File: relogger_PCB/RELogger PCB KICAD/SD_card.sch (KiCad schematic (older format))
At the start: 3 parts, among them J1 CON-SD-MMC-3, U1 4050

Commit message: Schematic uploaded with Arduino Nano, SD Card connector and DS3231 connector
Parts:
- removed J1: CON-SD-MMC-3, m-pad-2.1-DM1AA-SF-PEJ(21), symbol CON-SD-MMC-3
- removed R8: 10k, symbol R-RESCUE-RELogger_PCB_v1
- removed U1: 4050, symbol 4050
- added J3: CONN_01X06, symbol CONN_01X06
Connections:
- net labels added: MISO, MOSI, SCK, SD_CS
- net labels removed: CD, Vss
- wire segments 35 -> 7
- no-connect marks 7 -> 0
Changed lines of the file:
@@
 LIBS:matts_components
 LIBS:linear2
+LIBS:ds3231
+LIBS:micro_sd
 LIBS:RELogger_PCB_v1-cache
 EELAYER 25 0
@@
 Comment4 ""
 $EndDescr
-Wire Wire Line
-	6300 3800 6300 3650
-Wire Wire Line
-	3200 3300 4300 3300
-Wire Wire Line
-	6000 2950 6850 2950
-Wire Wire Line
-	6150 3050 6850 3050
-Wire Wire Line
-	6000 3250 6850 3250
-Wire Wire Line
-	3200 3900 4400 3900
-Wire Wire Line
-	5700 3150 6850 3150
-Wire Wire Line
-	5700 3150 5700 3900
-Wire Wire Line
-	3200 3600 6200 3600
-Wire Wire Line
-	6200 3600 6200 3350
-Wire Wire Line
-	6200 3350 6850 3350
-Wire Wire Line
-	3200 3000 4150 3000
-Wire Wire Line
-	6050 3650 6850 3650
-NoConn ~ 6850 3950
-NoConn ~ 6850 3850
-NoConn ~ 6850 3750
-NoConn ~ 6850 3450
-NoConn ~ 6850 3550
 $Comp
-L R-RESCUE-RELogger_PCB_v1 R8
-U 1 1 546255DF
-P 6300 4050
-F 0 "R8" V 6380 4050 50  0000 C CNN
-F 1 "10k" V 6300 4050 50  0000 C CNN
-F 2 "" H 6300 4050 60  0001 C CNN
-F 3 "" H 6300 4050 60  0001 C CNN
-	1    6300 4050
+L CONN_01X06 J3
+U 1 1 58F140FE
+P 6000 3450
+F 0 "J3" H 6000 3800 50  0000 C CNN
+F 1 "CONN_01X06" V 6100 3450 50  0000 C CNN
+F 2 "" H 6000 3450 50  0001 C CNN
+F 3 "" H 6000 3450 50  0001 C CNN
+	1    6000 3450
 	1    0    0    -1
 $EndComp
-$Comp
-L CON-SD-MMC-3 J1
-U 1 1 54625627
-P 7150 3350
-F 0 "J1" H 7000 4080 50  0000 L BNN
-F 1 "CON-SD-MMC-3" H 7100 2550 50  0000 L BNN
-F 2 "m-pad-2.1-DM1AA-SF-PEJ(21)" H 7150 3500 50  0001 C CNN
-F 3 "" H 7150 3350 60  0001 C CNN
-	1    7150 3350
-	1    0    0    -1
-$EndComp
-Text HLabel 3200 3000 0    60   Input ~ 0
+Text HLabel 5450 3200 0    60   Input ~ 0
+3V3
+Text HLabel 5450 3400 0    60   Input ~ 0
+D11
+Text HLabel 5450 3300 0    60   Input ~ 0
 D10
-Text HLabel 3200 3300 0    60   Input ~ 0
-D11
-Text HLabel 3200 3600 0    60   Input ~ 0
+Text HLabel 5450 3500 0    60   Input ~ 0
+D13
+Text HLabel 5450 3600 0    60   Input ~ 0
 D12
-Text HLabel 3200 3900 0    60   Input ~ 0
-D13
-Text HLabel 3150 2250 0    60   Input ~ 0
-3V3
+Text HLabel 5450 3850 3    60   Input ~ 0
+GND
+Text Label 5500 3300 0    60   ~ 0
+SD_CS
+Text Label 5500 3400 0    60   ~ 0
+MOSI
+Text Label 5500 3500 0    60   ~ 0
+SCK
+Text Label 5500 3600 0    60   ~ 0
+MISO
 Wire Wire Line
-	6150 1750 6150 3050
-Text HLabel 3150 4250 0    60   Output ~ 0
-CD
-$Comp
-L 4050 U1
-U 1 1 546524B9
-P 4850 2100
-F 0 "U1" H 5045 2215 60  0000 C CNN
-F 1 "4050" H 5040 1975 60  0000 C CNN
-F 2 "" H 4850 2100 60  0000 C CNN
-F 3 "" H 4850 2100 60  0000 C CNN
-	1    4850 2100
-	1    0    0    -1
-$EndComp
-$Comp
-L 4050 U1
-U 2 1 546524C8
-P 4850 2600
-F 0 "U1" H 5045 2715 60  0000 C CNN
-F 1 "4050" H 5040 2475 60  0000 C CNN
-F 2 "" H 4850 2600 60  0000 C CNN
-F 3 "" H 4850 2600 60  0000 C CNN
-	2    4850 2600
-	1    0    0    -1
-$EndComp
-$Comp
-L 4050 U1
-U 3 1 546524D7
-P 4850 3900
-F 0 "U1" H 5045 4015 60  0000 C CNN
-F 1 "4050" H 5040 3775 60  0000 C CNN
-F 2 "" H 4850 3900 60  0000 C CNN
-F 3 "" H 4850 3900 60  0000 C CNN
-	3    4850 3900
-	1    0    0    -1
-$EndComp
-$Comp
-L 4050 U1
-U 4 1 546524F0
-P 4850 4550
-F 0 "U1" H 5045 4665 60  0000 C CNN
-F 1 "4050" H 5040 4425 60  0000 C CNN
-F 2 "" H 4850 4550 60  0000 C CNN
-F 3 "" H 4850 4550 60  0000 C CNN
-	4    4850 4550
-	1    0    0    -1
-$EndComp
+	5450 3200 5800 3200
 Wire Wire Line
-	5950 2750 6850 2750
+	5450 3300 5800 3300
 Wire Wire Line
-	5950 2750 5950 2100
+	5450 3400 5800 3400
 Wire Wire Line
-	5950 2100 5300 2100
+	5450 3500 5800 3500
 Wire Wire Line
-	4150 3000 4150 2100
+	5450 3600 5800 3600
 Wire Wire Line
-	4150 2100 4400 2100
+	5450 3700 5450 3850
 Wire Wire Line
-	5700 2850 6850 2850
-Wire Wire Line
-	5700 2850 5700 2600
-Wire Wire Line
-	5700 2600 5300 2600
-Wire Wire Line
-	4300 3300 4300 2600
-Wire Wire Line
-	4300 2600 4400 2600
-Wire Wire Line
-	5700 3900 5300 3900
-Wire Wire Line
-	6150 1750 3600 1750
-Wire Wire Line
-	3600 1750 3600 2250
-Wire Wire Line
-	3600 2250 3150 2250
-Wire Wire Line
-	3150 4250 6050 4250
-Wire Wire Line
-	6050 4250 6050 3650
-Connection ~ 6300 3650
-Wire Wire Line
-	6300 4800 6300 4300
-Wire Wire Line
-	4800 2350 4800 2200
-Wire Wire Line
-	4800 2000 4800 1750
-Connection ~ 4800 1750
-NoConn ~ 4400 4550
-NoConn ~ 5300 4550
-Text HLabel 3150 4800 0    60   Input ~ 0
-Vss
-Wire Wire Line
-	3150 4800 6300 4800
-Text HLabel 6000 2950 0    60   Input ~ 0
-GND
-Text HLabel 6000 3250 0    60   Input ~ 0
-GND
-Text HLabel 4550 2350 0    60   Input ~ 0
-GND
-Wire Wire Line
-	4550 2350 4800 2350
+	5800 3700 5450 3700
 $EndSCHEMATC

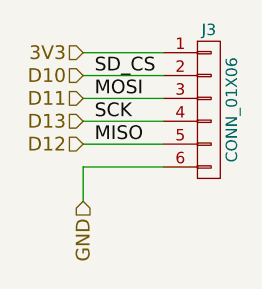
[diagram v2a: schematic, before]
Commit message: Schematic update and PCB initial run
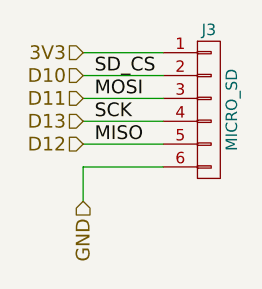
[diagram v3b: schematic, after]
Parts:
- J3: value CONN_01X06 -> MICRO_SD; footprint (none) -> REInnovationFootprint:TH_SD_MODULE
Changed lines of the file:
@@
 P 6000 3450
 F 0 "J3" H 6000 3800 50  0000 C CNN
-F 1 "CONN_01X06" V 6100 3450 50  0000 C CNN
-F 2 "" H 6000 3450 50  0001 C CNN
+F 1 "MICRO_SD" V 6100 3450 50  0000 C CNN
+F 2 "REInnovationFootprint:TH_SD_MODULE" H 6000 3450 50  0001 C CNN
 F 3 "" H 6000 3450 50  0001 C CNN
 	1    6000 3450
